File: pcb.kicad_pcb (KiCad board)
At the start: 4 copper layers, 32 x 45.8 mm, 63 parts, among them J1 USB_C_Receptacle_USB2.0, J2 OLED, Q1 2N7002, Q2 Si2301CDS, Q3 2N7002, Q4 Si2301CDS, SW1 SW_Push, U1 ADXL375, U2 ESP32-S3-MINI-1, U3 AMS1117-3.3, U4 MCP73831-2-OT, U5 W25Q128JVS

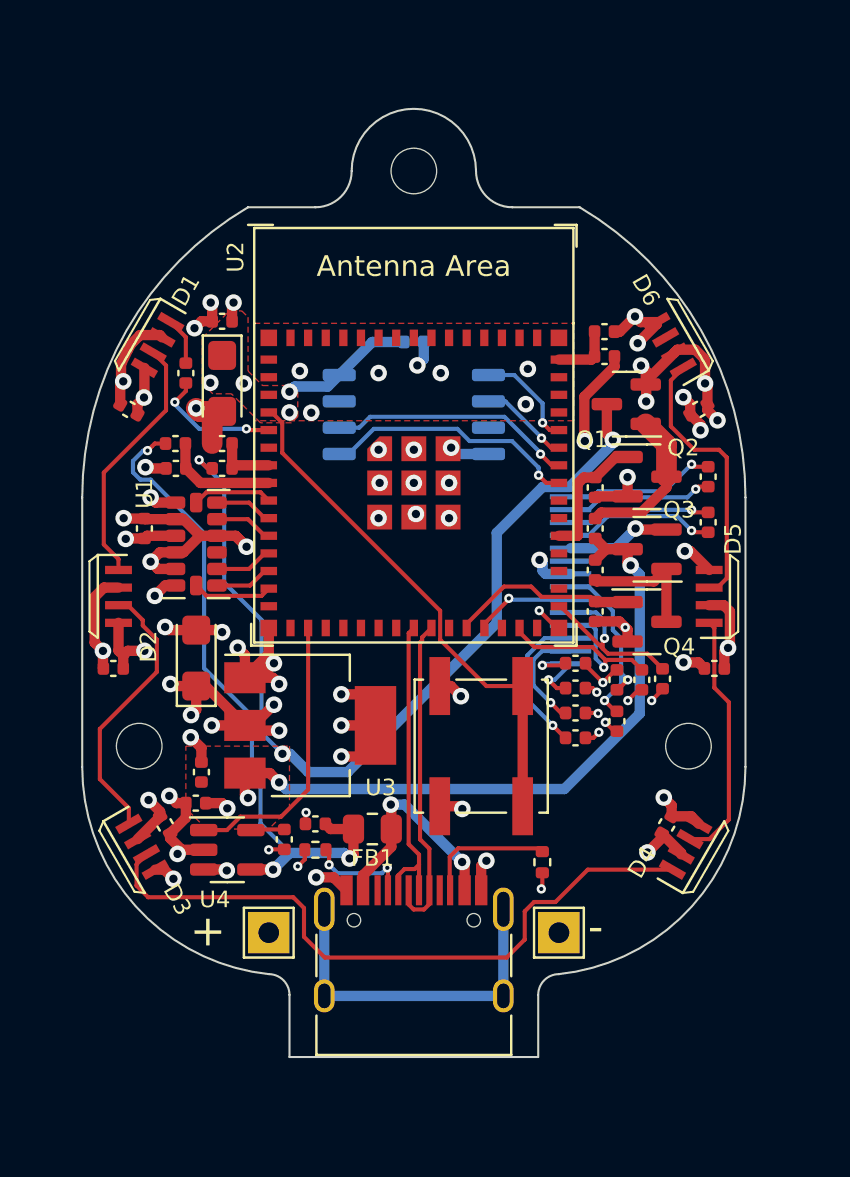
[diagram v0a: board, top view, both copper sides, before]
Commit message: Use bare ESP32 chip instead of module (#1)
* fixed library issues

* add submodules to CI/CD

* fix yaml syntax

* added part numbers

* Bare ESP layout

* fix erc/drc

* fix overlap

* added part numbers

* fixed layout
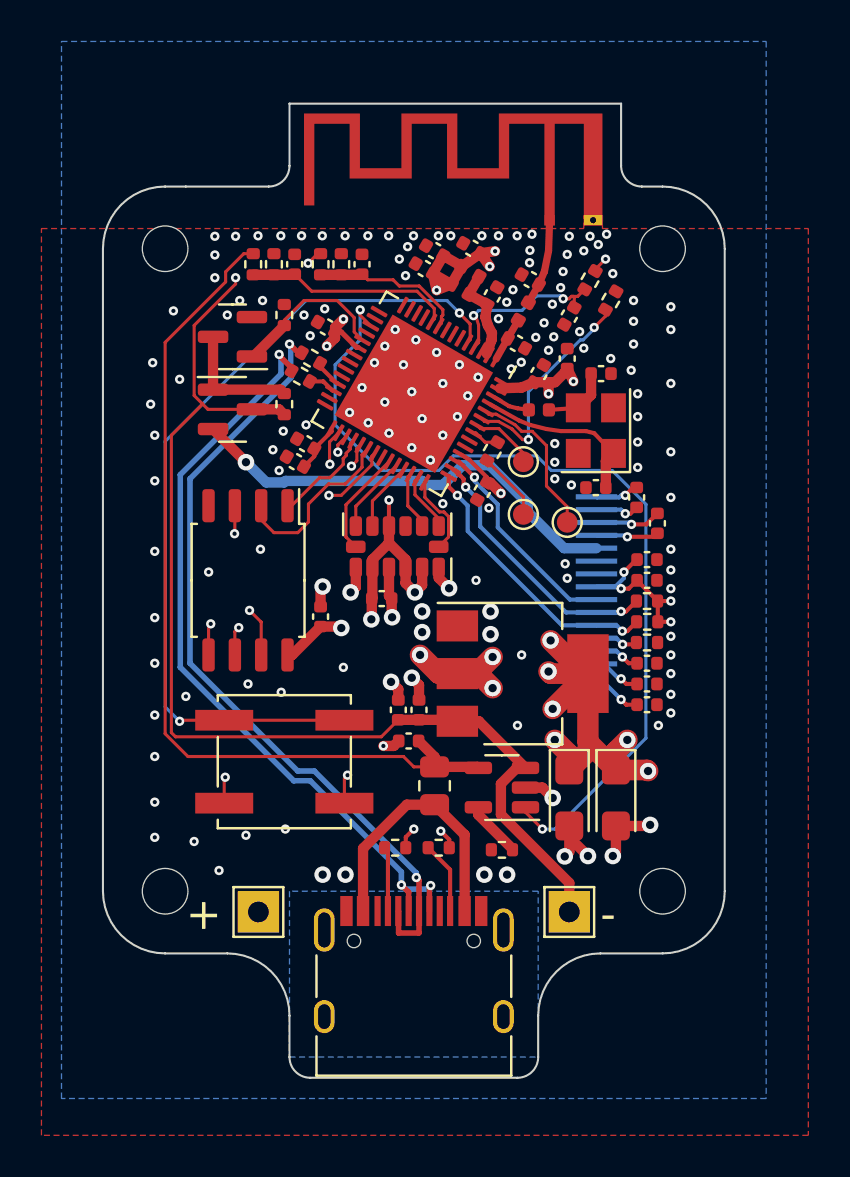
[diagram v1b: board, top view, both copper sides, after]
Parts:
- removed C1, C2, C21, C3, C4, C5, C6: 100n, Capacitor_SMD:C_0402_1005Metric
- removed C19: 1u, Capacitor_SMD:C_0402_1005Metric
- removed D1, D2, D3, D4, D5, D6: WS2812B-4020, WS2812B-4020:WS2812B-4020
- removed G***: LOGO, silkscreen-art:silkscreen-art
- removed Q1: 2N7002, Package_TO_SOT_SMD:SOT-23
- removed Q2: Si2301CDS, Package_TO_SOT_SMD:SOT-23
- removed R1, R12, R2: 10k, Capacitor_SMD:C_0402_1005Metric
- removed R4: 100, Capacitor_SMD:C_0402_1005Metric
- removed U2: ESP32-S3-MINI-1, PCM_Espressif:ESP32-S2-MINI-1
- added AE2: PCB Antenna, RF_Antenna:Texas_SWRA117D_2.4GHz_Left, F.Cu at (165.6, 58.6)
- added C23: 100n, Capacitor_SMD:C_0402_1005Metric, F.Cu at (162.3, 71.7)
- added C24: 100n, Capacitor_SMD:C_0402_1005Metric, F.Cu at (153.8, 69.4)
- added C25: 1u, Capacitor_SMD:C_0402_1005Metric, F.Cu at (153.3, 70.3)
- added C26: 100n, Capacitor_SMD:C_0402_1005Metric, F.Cu at (159.5, 61.0)
- added C27: 1u, Capacitor_SMD:C_0402_1005Metric, F.Cu at (161.8, 60.0)
- added C28: 10u, Capacitor_SMD:C_0402_1005Metric, F.Cu at (160.0, 60.1)
- added C29: 100n, Capacitor_SMD:C_0402_1005Metric, F.Cu at (162.8, 62.3)
- added C30: 10u, Capacitor_SMD:C_0402_1005Metric, F.Cu at (166.4, 65.3)
- added C31: 1u, Capacitor_SMD:C_0402_1005Metric, F.Cu at (165.0, 66.0)
- added C32: 100n, Capacitor_SMD:C_0402_1005Metric, F.Cu at (154.8, 63.8)
- added C33: 1u, Capacitor_SMD:C_0402_1005Metric, F.Cu at (166.5, 63.2)
- added C34: 22p, Capacitor_SMD:C_0402_1005Metric, F.Cu at (168.0, 66.0)
- added C35: 22p, Capacitor_SMD:C_0402_1005Metric, F.Cu at (167.8, 71.5)
- added C36: 4p7, Capacitor_SMD:C_0402_1005Metric, F.Cu at (163.9, 64.6)
- added C37: 3p3, Capacitor_SMD:C_0402_1005Metric, F.Cu at (164.6, 61.5)
- added C38: 100n, Capacitor_SMD:C_0402_1005Metric, F.Cu at (153.2, 60.8)
- added C39: 100n, Capacitor_SMD:C_0402_1005Metric, F.Cu at (156.5, 60.8)
- added H4: MountingHole, MountingHole:MountingHole_2.2mm_M2, F.Cu at (147.0, 91.0)
- added L1: 3.9nH, Inductor_SMD:L_0402_1005Metric, F.Cu at (161.2, 62.0)
- added L2: 3.9nH, Inductor_SMD:L_0402_1005Metric, F.Cu at (161.7, 61.1)
- added L3: 15nH, Inductor_SMD:L_0402_1005Metric, F.Cu at (165.0, 67.8)
- added L4: 1.8nH, Inductor_SMD:L_0402_1005Metric, F.Cu at (164.3, 63.0)
- added R13: 10k, Resistor_SMD:R_0402_1005Metric, F.Cu at (168.5, 62.5)
- added R14: 10k, Resistor_SMD:R_0402_1005Metric, F.Cu at (167.5, 61.5)
- added R20: 470, Resistor_SMD:R_0402_1005Metric, F.Cu at (162.8, 69.8)
- added R21: 0R, Resistor_SMD:R_0402_1005Metric, F.Cu at (153.5, 66.1)
- added R22: 0R, Resistor_SMD:R_0402_1005Metric, F.Cu at (154.0, 65.3)
- added TP3: TXD, TestPoint:TestPoint_Pad_D1.0mm, F.Cu at (164.3, 72.8)
- added TP4: RXD, TestPoint:TestPoint_Pad_D1.0mm, F.Cu at (164.3, 70.3)
- added TP5: BOOT1, TestPoint:TestPoint_Pad_D1.0mm, F.Cu at (166.4, 73.2)
- added U6: ESP32-S3, Package_DFN_QFN:QFN-56-1EP_7x7mm_P0.4mm_EP5.6x5.6mm, F.Cu at (159.0, 67.0)
- added Y1: 40MHz 15pF, Crystal:Crystal_SMD_3225-4Pin_3.2x2.5mm, F.Cu at (167.8, 68.8)
- C22, U5: moved to F.Cu
- R10, R11: value 4k7 -> 10k; footprint Capacitor_SMD:C_0402_1005Metric -> Resistor_SMD:R_0402_1005Metric
- R15, R16, R17, R18: value 100k -> 120k; footprint Capacitor_SMD:C_0402_1005Metric -> Resistor_SMD:R_0402_1005Metric
- R3, R5, R8, R9: footprint Capacitor_SMD:C_0402_1005Metric -> Resistor_SMD:R_0402_1005Metric
- moved H2 26.2 mm to (171.0, 91.0)
- moved C20 26.1 mm to (166.5, 86.5)
- moved Q3 24.3 mm to (150.2, 64.2), turned to 180 degrees
- moved H1 24.0 mm to (171.0, 60.0)
- moved C8 21.3 mm to (168.8, 86.5), turned to -90 degrees
- moved Q4 21.1 mm to (150.2, 67.8), turned to 0 degrees
- moved R3 20.7 mm to (152.8, 63.2), turned to 90 degrees
- moved R8 17.0 mm to (152.8, 67.5), turned to 90 degrees
- moved TP1 14.5 mm to (166.5, 92.0), turned to -90 degrees
- moved TP2 14.5 mm to (151.5, 92.0), turned to -90 degrees
- moved C22 14.0 mm to (154.5, 77.8), turned to 90 degrees
- moved U4 13.6 mm to (163.2, 86.0), turned to 180 degrees
- moved H3 12.6 mm to (147.0, 60.0)
- moved C10 11.9 mm to (157.4, 76.9), turned to 180 degrees
- moved C9 11.7 mm to (159.2, 82.2), turned to 90 degrees
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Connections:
- U5 pad 2: FLASH-SDO -> FLASH-Q
- U5 pad 3: unconnected-(U5-IO2-Pad3) -> FLASH-WP
- U5 pad 5: FLASH-SDI -> FLASH-D
- U5 pad 6: FLASH-SCK -> FLASH-CLK
- U5 pad 7: unconnected-(U5-IO3-Pad7) -> FLASH-HD
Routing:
- net GND: track 78.2 -> 27.2 mm, vias 58 -> 156
- net Net-(D3-DOUT): track 32.4 -> 0.00 mm
- net CHARGE_STAT: track 13.6 -> 43.7 mm, vias 0 -> 2
- net /LEDs/VLED: track 27.8 -> 0.00 mm, vias 9 -> 0
- net VBAT: track 86.6 -> 59.8 mm, vias 8 -> 2
- net USB_D-: track 14.9 -> 38.3 mm, vias 0 -> 2
- net USB_D+: track 15.6 -> 37.8 mm, vias 0 -> 3
- net +3.3V: track 46.1 -> 64.7 mm, vias 21 -> 26
- net unconnected-(J1-SHIELD-PadS1): track 17.0 -> 0.00 mm
- net /OLED/OLED-VBAT: track 5.04 -> 22.0 mm
- net /BOOT: track 25.2 -> 40.7 mm, vias 0 -> 2
- net FLASH-D: track 0.00 -> 13.4 mm, vias 0 -> 2
- net Net-(D2-DOUT): track 13.3 -> 0.00 mm
- net Net-(D5-DOUT): track 13.3 -> 0.00 mm
- net FLASH-HD: track 0.00 -> 13.2 mm, vias 0 -> 2
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- added copper zone on B.Cu, net GND
- added copper zone on B.Cu, net unconnected-(J1-SHIELD-PadS1)
- removed copper zone on F.Cu, net +3.3V
- removed copper zone on In2.Cu, net /LEDs/VLED
- removed copper zone on F.Cu, net VBAT
- removed copper zone on In2.Cu, net VBAT
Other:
- board size 32 x 45.8 mm -> 30 x 47 mm

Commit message: Incorporate feedback from cnlohr
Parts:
- added R1: 10k, Resistor_SMD:R_0402_1005Metric, F.Cu at (155.8, 80.8)
- moved TP3 2.28 mm to (162.8, 74.5)
- moved TP5 1.91 mm to (165.0, 74.5)
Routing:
- net Net-(R20-Pad2): track 3.33 -> 5.62 mm
- net /BOOT: track 40.7 -> 43.0 mm
- net Net-(U6-GPIO46): track 7.64 -> 8.69 mm
- net +3.3V: track 64.7 -> 65.4 mm, vias 26 -> 27
- net GND: vias 156 -> 155
